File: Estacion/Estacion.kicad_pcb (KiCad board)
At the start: 2 copper layers, 120 x 100 mm, 6 parts, among them U4 WeMos_S2_mini, U5 DHT22, U6 FN-M16P

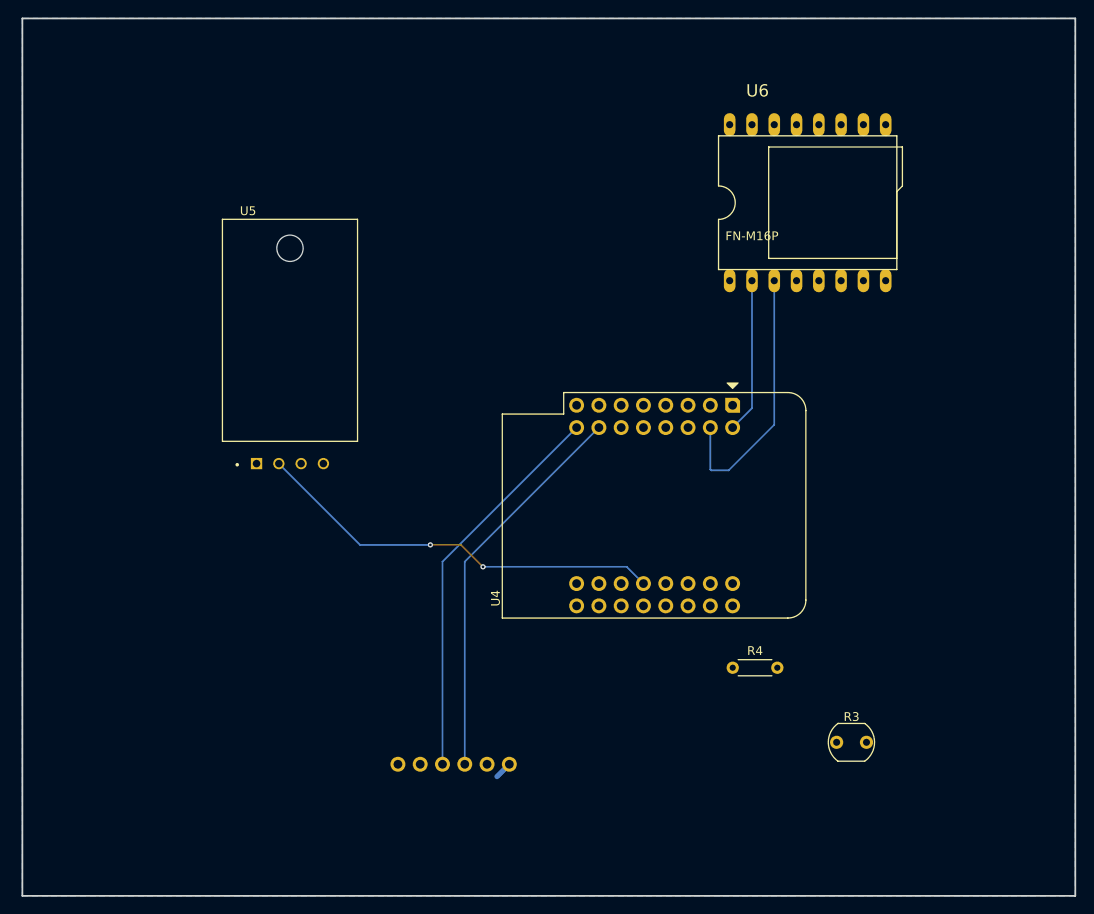
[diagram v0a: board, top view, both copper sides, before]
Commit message: terminar pantalla y leds
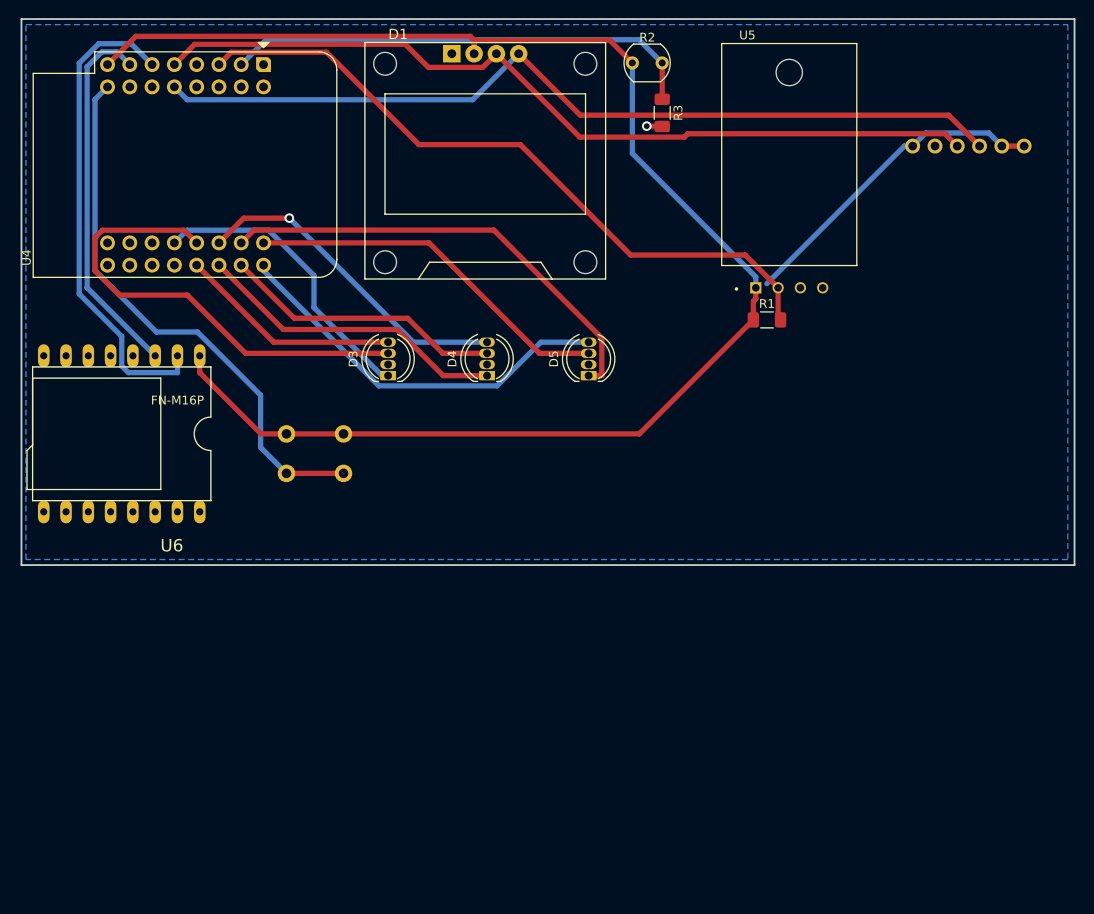
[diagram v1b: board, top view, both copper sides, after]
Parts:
- removed R4: R_US, Resistor_THT:R_Axial_DIN0204_L3.6mm_D1.6mm_P5.08mm_Horizontal
- added D1: OLED Display, especificos:OLED-Display_SSD1306_128x64, F.Cu at (117.8, 68.7)
- added D3: LED_RABG, LED_THT:LED_D5.0mm-4_RGB, F.Cu at (106.7, 92.7)
- added D4: LED_RABG, LED_THT:LED_D5.0mm-4_RGB, F.Cu at (118.0, 92.7)
- added D5: LED_RABG, LED_THT:LED_D5.0mm-4_RGB, F.Cu at (129.5, 92.7)
- added R1: 10k, Resistor_SMD:R_1206_3216Metric_Pad1.30x1.75mm_HandSolder, F.Cu at (149.9, 86.4)
- added R2: LDR07, OptoDevice:R_LDR_5.1x4.3mm_P3.4mm_Vertical, F.Cu at (134.5, 57.1)
- added SW1: SW_Push, Button_Switch_THT:SW_PUSH_6mm, B.Cu at (101.6, 99.3)
- R3: value LDR07 -> 10k; footprint OptoDevice:R_LDR_5.1x4.3mm_P3.4mm_Vertical -> Resistor_SMD:R_1206_3216Metric_Pad1.30x1.75mm_HandSolder
- moved BMP280 84.1 mm to (166.5, 66.5), turned to 90 degrees
- moved U6 82.5 mm to (76.3, 99.3), turned to 180 degrees
- moved R3 74.4 mm to (137.9, 62.8), turned to -90 degrees
- moved U4 66.1 mm to (92.5, 57.3)
- moved U5 60.3 mm to (152.4, 67.5)
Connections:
- BMP280 pad 1: Net-(BMP280-VCC) -> +3V3
- BMP280 pad 3: Net-(BMP280-SCL) -> /SCL
- BMP280 pad 4: Net-(BMP280-SDA) -> /SDA
- BMP280 pad 5: unconnected-(BMP280-CSB-Pad5) -> +3V3
- BMP280 pad 6: unconnected-(BMP280-SDO-Pad6) -> +3V3
- R3 pad 1: Net-(U4-VBUS) -> Net-(U4-GPIO3)
- R3 pad 2: Net-(U4-GPIO39) -> GND
- U4 pad 13: unconnected-(U4-GPIO33-Pad13) -> Net-(D3-GK)
- U4 pad 14: unconnected-(U4-GPIO35-Pad14) -> Net-(D4-RK)
- U4 pad 15: unconnected-(U4-GPIO37-Pad15) -> Net-(D4-BK)
- U4 pad 16: Net-(U4-GPIO39) -> Net-(D5-GK)
- U4 pad 17: Net-(U4-GPIO1) -> unconnected-(U4-GPIO1-Pad17)
- U4 pad 18: Net-(U4-GPIO2) -> unconnected-(U4-GPIO2-Pad18)
- U4 pad 2: unconnected-(U4-GPIO3-Pad2) -> Net-(U4-GPIO3)
- U4 pad 21: unconnected-(U4-GPIO8-Pad21) -> /SDA
- U4 pad 23: Net-(BMP280-SCL) -> unconnected-(U4-GPIO13-Pad23)
- U4 pad 24: Net-(BMP280-SDA) -> Net-(U4-GPIO14)
- U4 pad 28: Net-(U4-GPIO21) -> Net-(D3-RK)
- U4 pad 29: unconnected-(U4-GPIO34-Pad29) -> Net-(D3-BK)
- U4 pad 3: unconnected-(U4-GPIO5-Pad3) -> Net-(U4-GPIO5)
- U4 pad 30: unconnected-(U4-GPIO36-Pad30) -> Net-(D4-GK)
- U4 pad 31: unconnected-(U4-GPIO38-Pad31) -> Net-(D5-RK)
- U4 pad 32: unconnected-(U4-GPIO40-Pad32) -> Net-(D5-BK)
- U4 pad 5: unconnected-(U4-GPIO9-Pad5) -> /SCL
- U4 pad 6: unconnected-(U4-GPIO11-Pad6) -> Net-(U4-GPIO11)
- U4 pad 7: unconnected-(U4-GPIO12-Pad7) -> Net-(U4-GPIO12)
- U4 pad 8: Net-(BMP280-VCC) -> +3V3
- U4 pad 9: Net-(U4-VBUS) -> +5V
- U5 pad 1: Net-(BMP280-VCC) -> +3V3
- U5 pad 2: Net-(U4-GPIO21) -> Net-(U4-GPIO5)
- U6 pad 1: Net-(BMP280-VCC) -> +3V3
- U6 pad 2: Net-(U4-GPIO1) -> Net-(U4-GPIO11)
- U6 pad 3: Net-(U4-GPIO2) -> Net-(U4-GPIO12)
- U6 pad 7: unconnected-(U6-GND@-Pad7) -> GND
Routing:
- net +3V3: track 0.00 -> 209.5 mm
- net /SDA: track 0.00 -> 98.9 mm
- net /SCL: track 0.00 -> 96.6 mm
- net Net-(U4-GPIO5): track 0.00 -> 79.2 mm
- net Net-(U4-GPIO14): track 0.00 -> 62.9 mm
- net Net-(U4-GPIO11): track 0.00 -> 55.3 mm
- net Net-(U4-GPIO3): track 0.00 -> 54.4 mm
- net Net-(D3-BK): track 0.00 -> 53.6 mm
- net Net-(D5-RK): track 0.00 -> 52.6 mm
- net Net-(U4-GPIO21): track 47.2 -> 0.00 mm, vias 2 -> 0
- net Net-(D5-GK): track 0.00 -> 45.2 mm
- net Net-(BMP280-SCL): track 44.7 -> 0.00 mm
- net Net-(BMP280-SDA): track 44.7 -> 0.00 mm
- net Net-(U4-GPIO12): track 0.00 -> 42.3 mm
- net Net-(D5-BK): track 0.00 -> 42.3 mm
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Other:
- board size 120 x 100 mm -> 120 x 62.2 mm
